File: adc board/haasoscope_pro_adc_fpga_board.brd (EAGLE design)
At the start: 220 x 160 mm, 564 parts, among them CN2 12Vin, IC1 ADC12DL2500ACF, IC13 LMH5401IRMST, IC14 LMH6401IRMZR, IC15 SN74AVC4T774PWR, IC17 DAC8562SDGSR, IC18 TLV9102IPWR, IC2 SN74AVC4T774PWR, IC21 LMH5401IRMST, IC22 TPS7A7200RGTR, IC23 TPS7A7200RGTR, IC24 TPS7A7200RGTR, IC25 TPS72325DBVR, IC26 TPS7A7200RGTR, IC27 TPS7A7200RGTR, IC28 TPS7A7200RGTR, IC29 LMH6401IRMZR, IC3 ADC122S021CIMM_NOPB, IC30 SN74AVC4T774PWR, IC33 TLV9102IPWR, IC4 TLV9102IPWR, IC5 EP4CE30F23C6N, IC6 EPCQ16ASI8N, IC8 FT232HQ, IC9 93LC56B, J1 2p-2.54, J10 8pin, J11 8pin, J13 8pin, J14 2x5, J15 test1, J2 test1, J30 2p-2.54, J31 2p-2.54, J32 2p-2.54, J33 2p-2.54, J34 2p-2.54, J35 2p-2.54, J36 2p-2.54, J37 2p-2.54, J39 2p-2.54, J40 2p-2.54, J41 2p-2.54, J42 2p-2.54, J43 2p-2.54, J44 2p-2.54, J45 2p-2.54, J46 2p-2.54, J8 8pin, K10 G6K-2F-RF-DC3, K11 G6K-2F-RF-DC3, K12 G6K-2F-RF-DC3, K5 AQY21SOP, K6 G6K-2F-RF-DC3, K7 G6K-2F-RF-DC3, K9 AQY21SOP, Q1 S8050, Q4 S8050, Q5 S8050, Q7 S8050, Q8 S8050, Q9 S8050, SW3 SKQGADE010, SW4 SKQGADE010, U2 ADF4350BCPZ, U6 AMS1117-1.2, X1 USBC, Y2 OSCILLATORSMD-5X3, Y3 12MHz

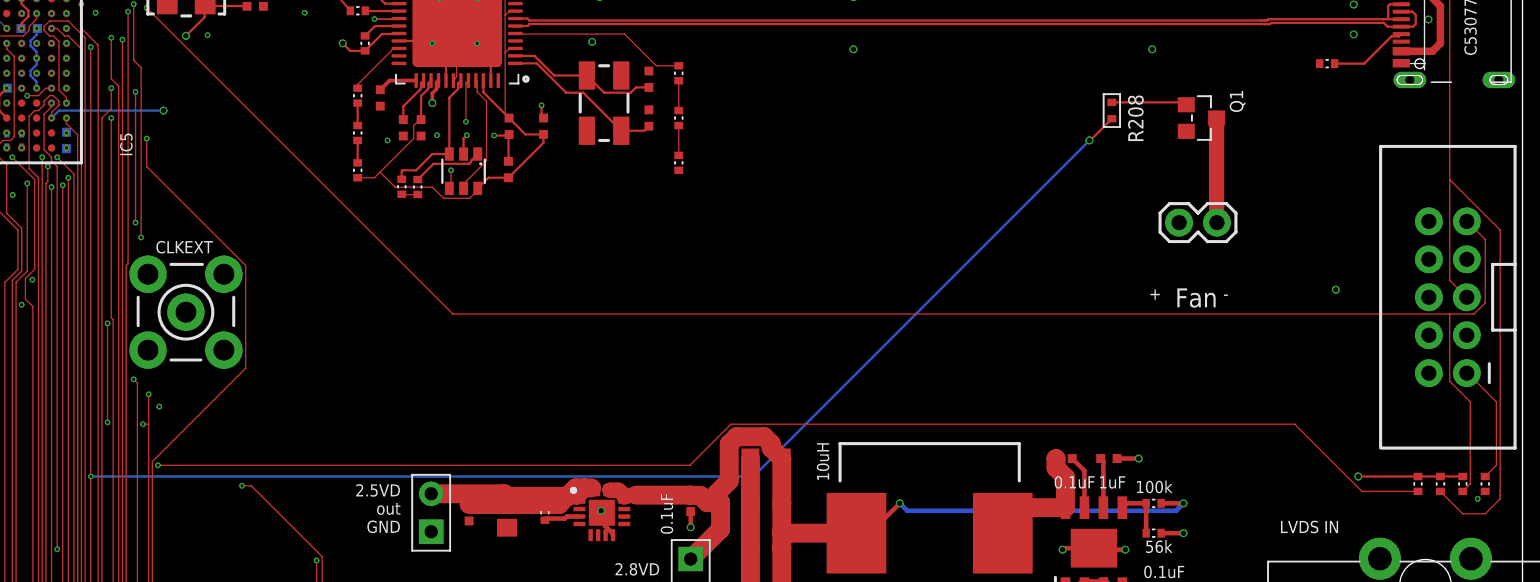
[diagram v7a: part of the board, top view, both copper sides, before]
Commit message: Move fan connector a bit away from USB lines
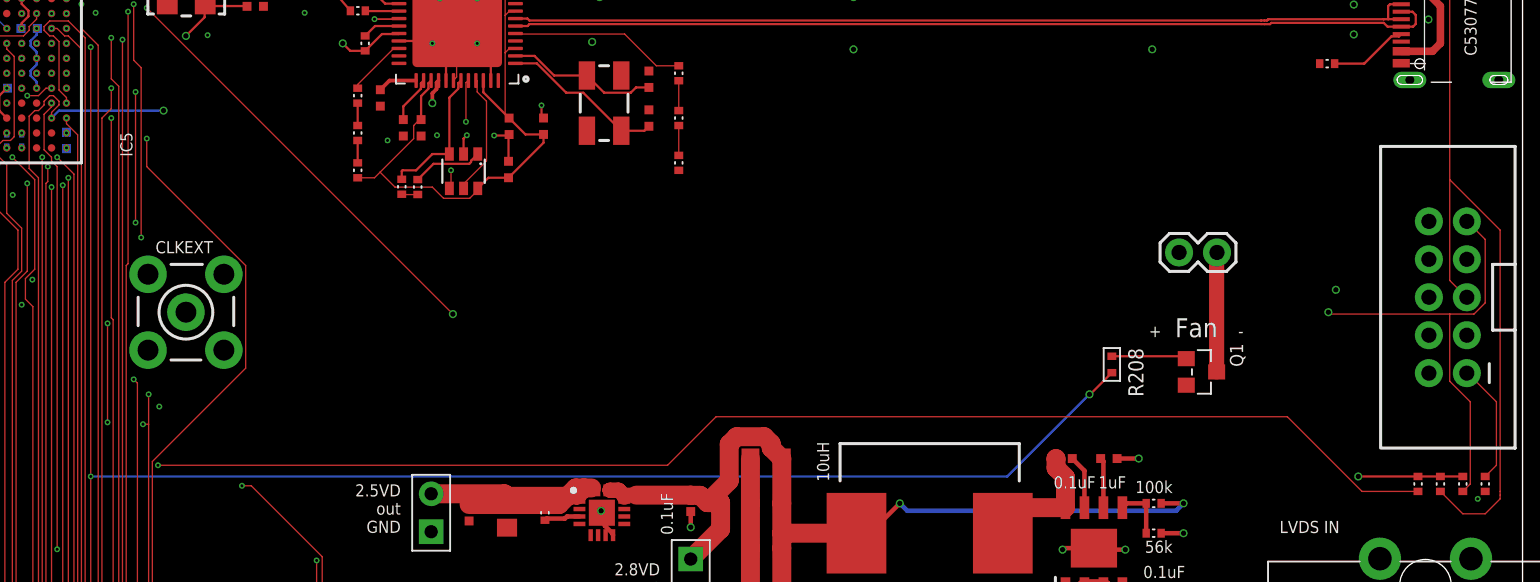
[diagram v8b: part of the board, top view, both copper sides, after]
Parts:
- moved Q1 17.0 mm to (198.5, 54.0)
- moved R208 17.0 mm to (192.5, 54.5)
- moved JST_FAN 2.00 mm to (197.0, 62.0)
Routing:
- net FAN_CONTROL: track 181.9 -> 174.9 mm
- net FAN-: track 7.01 -> 8.01 mm
- net TDI: track 137.9 -> 138.0 mm, vias 3 -> 5
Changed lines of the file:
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@@
 <drawing>
 <settings>
-<setting alwaysvectorfont="no"/>
+<setting alwaysvectorfont="yes"/>
 <setting verticaltext="up"/>
 </settings>
@@
 <wire x1="97.5" y1="40.5" x2="99" y2="39" width="0.1524" layer="21"/>
 <wire x1="99" y1="39" x2="99" y2="38.5" width="0.1524" layer="21"/>
-<text x="195.818" y="59.645" size="0.8128" layer="21" rot="R180">+</text>
-<text x="200.318" y="59.645" size="0.8128" layer="21" rot="R180">-</text>
+<text x="195.818" y="57.145" size="0.8128" layer="21" rot="R180">+</text>
+<text x="201.318" y="57.145" size="0.8128" layer="21" rot="R180">-</text>
 </plain>
 <attributes>
@@
 <attribute name="VALUE" x="104.605" y="97.435" size="0.8128" layer="21" rot="R180"/>
 </element>
-<element name="Q1" library="Seeed-Transistor" library_urn="urn:adsk.eagle:library:477" package="SOT-23" package3d_urn="urn:adsk.eagle:package:33015/1" value="S8050" x="198.5" y="71" smashed="yes" rot="R270">
-<attribute name="LCSC" value="C7420370" x="205.5" y="76" size="1.778" layer="27" rot="R270" display="off"/>
-<attribute name="MPN" value="S8050" x="205.5" y="76" size="1.778" layer="27" rot="R270" display="off"/>
-<attribute name="NAME" x="200.405" y="72.905" size="0.889" layer="25" rot="R270"/>
-<attribute name="VALUE" x="195.706" y="72.27" size="0.635" layer="27" rot="R270"/>
-</element>
-<element name="R208" library="MF_Passives" package="R0402" value="1k" x="192.5" y="71.5" smashed="yes" rot="R270">
-<attribute name="HOUSEPART" value="" x="199" y="76.5" size="1.778" layer="27" rot="R270" display="off"/>
-<attribute name="MPN" value="" x="199" y="76.5" size="1.778" layer="27" rot="R270" display="off"/>
-<attribute name="NAME" x="193.6" y="72.6" size="1.016" layer="25" font="vector" rot="R270"/>
-<attribute name="POPULATE" value="1" x="199" y="76.5" size="1.778" layer="27" rot="R270" display="off"/>
-<attribute name="TOLERANCE" value="" x="199" y="76.5" size="1.778" layer="27" rot="R270" display="off"/>
-<attribute name="URL" value="" x="199" y="76.5" size="1.778" layer="27" rot="R270" display="off"/>
-<attribute name="VOLTAGE" value="" x="199" y="76.5" size="1.778" layer="27" rot="R270" display="off"/>
-<attribute name="WATTAGE" value="" x="199" y="76.5" size="1.778" layer="27" rot="R270" display="off"/>
+<element name="Q1" library="Seeed-Transistor" library_urn="urn:adsk.eagle:library:477" package="SOT-23" package3d_urn="urn:adsk.eagle:package:33015/1" value="S8050" x="198.5" y="54" smashed="yes" rot="R270">
+<attribute name="LCSC" value="C7420370" x="205.5" y="59" size="1.778" layer="27" rot="R270" display="off"/>
+<attribute name="MPN" value="S8050" x="205.5" y="59" size="1.778" layer="27" rot="R270" display="off"/>
+<attribute name="NAME" x="200.405" y="55.905" size="0.889" layer="25" rot="R270"/>
+<attribute name="VALUE" x="195.706" y="55.27" size="0.635" layer="27" rot="R270"/>
+</element>
+<element name="R208" library="MF_Passives" package="R0402" value="1k" x="192.5" y="54.5" smashed="yes" rot="R270">
+<attribute name="HOUSEPART" value="" x="199" y="59.5" size="1.778" layer="27" rot="R270" display="off"/>
+<attribute name="MPN" value="" x="199" y="59.5" size="1.778" layer="27" rot="R270" display="off"/>
+<attribute name="NAME" x="193.6" y="55.6" size="1.016" layer="25" font="vector" rot="R270"/>
+<attribute name="POPULATE" value="1" x="199" y="59.5" size="1.778" layer="27" rot="R270" display="off"/>
+<attribute name="TOLERANCE" value="" x="199" y="59.5" size="1.778" layer="27" rot="R270" display="off"/>
+<attribute name="URL" value="" x="199" y="59.5" size="1.778" layer="27" rot="R270" display="off"/>
+<attribute name="VOLTAGE" value="" x="199" y="59.5" size="1.778" layer="27" rot="R270" display="off"/>
+<attribute name="WATTAGE" value="" x="199" y="59.5" size="1.778" layer="27" rot="R270" display="off"/>
 </element>
-<element name="JST_FAN" library="SparkFun-Connectors" package="1X02" value="Fan" x="197" y="64" smashed="yes">
-<attribute name="VALUE" x="196.73" y="58.325" size="1.27" layer="21"/>
+<element name="JST_FAN" library="SparkFun-Connectors" package="1X02" value="Fan" x="197" y="62" smashed="yes">
+<attribute name="VALUE" x="196.73" y="56.325" size="1.27" layer="21"/>
 </element>
 </elements>
@@
 <via x="124.125" y="75.75" extent="1-16" drill="0.2"/>
 <contactref element="R208" pad="P$2"/>
-<wire x1="192.5" y1="70.95" x2="191.05" y2="69.5" width="0.1524" layer="1"/>
-<wire x1="191.05" y1="69.5" x2="191" y2="69.5" width="0.1524" layer="1"/>
-<via x="191" y="69.5" extent="1-16" drill="0.35"/>
-<wire x1="168.5" y1="47" x2="124.125" y2="47" width="0.1524" layer="16"/>
+<wire x1="192.5" y1="53.95" x2="191.05" y2="52.5" width="0.1524" layer="1"/>
+<wire x1="191.05" y1="52.5" x2="191" y2="52.5" width="0.1524" layer="1"/>
+<via x="191" y="52.5" extent="1-16" drill="0.35"/>
+<wire x1="185.5" y1="47" x2="124.125" y2="47" width="0.1524" layer="16"/>
 <via x="124.125" y="47" extent="1-16" drill="0.2"/>
-<wire x1="191" y1="69.5" x2="168.5" y2="47" width="0.1524" layer="16"/>
+<wire x1="191" y1="52.5" x2="185.5" y2="47" width="0.1524" layer="16"/>
 </signal>
 <signal name="DEBUGOUT10">
@@
 <wire x1="126" y1="47.75" x2="111.125" y2="62.625" width="0.0889" layer="14"/>
 <wire x1="128.625" y1="47.75" x2="126" y2="47.75" width="0.0889" layer="14"/>
-<wire x1="164.25" y1="47.75" x2="128.625" y2="47.75" width="0.0889" layer="1"/>
-<wire x1="167" y1="50.5" x2="164.25" y2="47.75" width="0.0889" layer="1"/>
-<wire x1="204.75" y1="50.5" x2="167" y2="50.5" width="0.0889" layer="1"/>
-<wire x1="209.25" y1="46" x2="204.75" y2="50.5" width="0.0889" layer="1"/>
+<wire x1="162.75" y1="47.75" x2="128.625" y2="47.75" width="0.0889" layer="1"/>
+<wire x1="166" y1="51" x2="162.75" y2="47.75" width="0.0889" layer="1"/>
+<wire x1="204.25" y1="51" x2="166" y2="51" width="0.0889" layer="1"/>
+<wire x1="209.25" y1="46" x2="204.25" y2="51" width="0.0889" layer="1"/>
 <wire x1="213" y1="46" x2="209.25" y2="46" width="0.0889" layer="1"/>
 <via x="128.625" y="47.75" extent="1-16" drill="0.2"/>
@@
 <wire x1="148.375" y1="57.875" x2="127.875" y2="78.375" width="0.0889" layer="1"/>
 <wire x1="216.75" y1="57.875" x2="215.125" y2="57.875" width="0.0889" layer="1"/>
-<wire x1="215.125" y1="57.875" x2="148.375" y2="57.875" width="0.0889" layer="1"/>
 <wire x1="217.5" y1="58.625" x2="216.75" y2="57.875" width="0.0889" layer="1"/>
 <wire x1="217.5" y1="62.875" x2="217.5" y2="58.625" width="0.0889" layer="1"/>
@@
 <via x="123.75" y="82.5" extent="1-16" drill="0.2"/>
 <via x="127.875" y="78.375" extent="1-16" drill="0.2"/>
+<wire x1="215.125" y1="57.875" x2="207.125" y2="57.875" width="0.0889" layer="1"/>
+<wire x1="207.125" y1="57.875" x2="207" y2="58" width="0.0889" layer="1"/>
+<via x="207" y="58" extent="1-16" drill="0.35"/>
+<wire x1="207" y1="58" x2="148.5" y2="58" width="0.0889" layer="3"/>
+<wire x1="148.5" y1="58" x2="148.375" y2="57.875" width="0.0889" layer="3"/>
+<via x="148.375" y="57.875" extent="1-16" drill="0.35"/>
 </signal>
 <signal name="IO149">
@@
 <contactref element="Q1" pad="1"/>
 <contactref element="R208" pad="P$1"/>
-<wire x1="192.5" y1="72.05" x2="197.323" y2="72.05" width="0.1524" layer="1"/>
-<wire x1="197.323" y1="72.05" x2="197.484" y2="71.889" width="0.1524" layer="1"/>
+<wire x1="192.5" y1="55.05" x2="197.323" y2="55.05" width="0.1524" layer="1"/>
+<wire x1="197.323" y1="55.05" x2="197.484" y2="54.889" width="0.1524" layer="1"/>
 </signal>
 <signal name="FAN-">
 <contactref element="Q1" pad="3"/>
 <contactref element="JST_FAN" pad="2"/>
-<wire x1="199.54" y1="64" x2="199.516" y2="64.024" width="1.016" layer="1"/>
-<wire x1="199.516" y1="64.024" x2="199.516" y2="71" width="1.016" layer="1"/>
+<wire x1="199.54" y1="62" x2="199.516" y2="61.976" width="1.016" layer="1"/>
+<wire x1="199.516" y1="61.976" x2="199.516" y2="54" width="1.016" layer="1"/>
 </signal>
 </signals>
